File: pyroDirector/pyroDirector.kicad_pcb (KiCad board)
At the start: 2 copper layers, 100 x 100 mm, 92 parts, among them J1 AudioJack3.5mm, J10 PWR_CONN, J11 CALIB_MODULE, J12 DISP_I2C, J13 Conn_01x03_Male, J14 SJ1-2503A, J15 Conn_01x03_Male, J16 SJ1-2503A, J17 Conn_01x03_Male, J18 SJ1-2503A, J19 LED_ext, J2 Header_A1-A15, J20 Screw_Terminal_01x02, J21 LED_ext, J22 Screw_Terminal_01x02, J23 LED_ext, J24 Screw_Terminal_01x02, J3 Header_D14-19, J4 Header_D48-53, J5 V_Batt, J6 Header_ISP, J7 PWR_SWITCH, J8 Batt, J9 Conn_01x07_Male, K1 PR12-5V-360-1C, K2 PR12-5V-360-1C, K3 PR12-5V-360-1C, Q1 MMBT2222A 1P, Q10 MMBT2222A 1P, Q11 IRLB8721PbF, Q12 MMBT2222A 1P, Q13 IRLB8721PbF, Q2 MMBT2222A 1P, Q3 MMBT2222A 1P, Q4 MMBT2222A 1P, Q5 MMBT2222A 1P, Q6 MMBT2222A 1P, Q7 MMBT2222A 1P, Q8 MMBT2222A 1P, Q9 IRLB8721PbF, SW1 SW_SPDT, U1 MEGA_PRO_ATMEGA2560

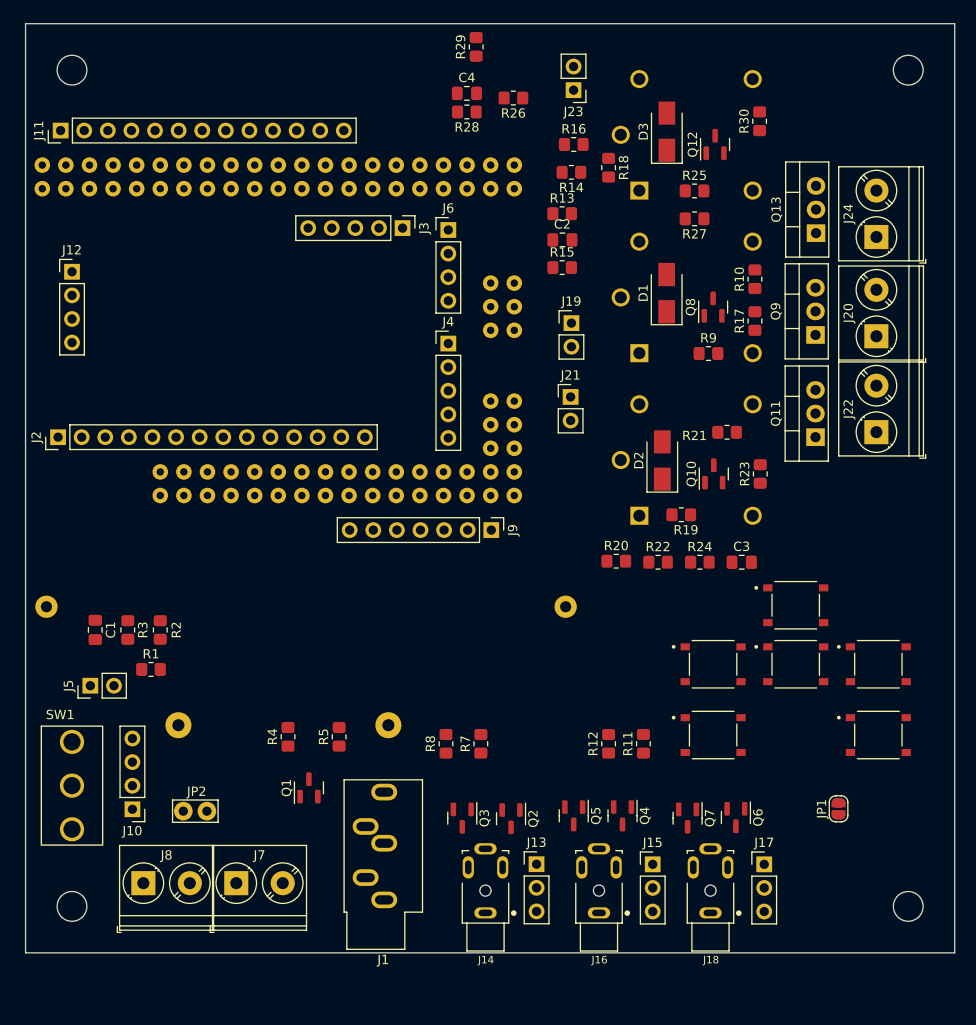
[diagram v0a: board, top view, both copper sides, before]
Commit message: placement improvements, added missing header -->should we use handsolder pads?
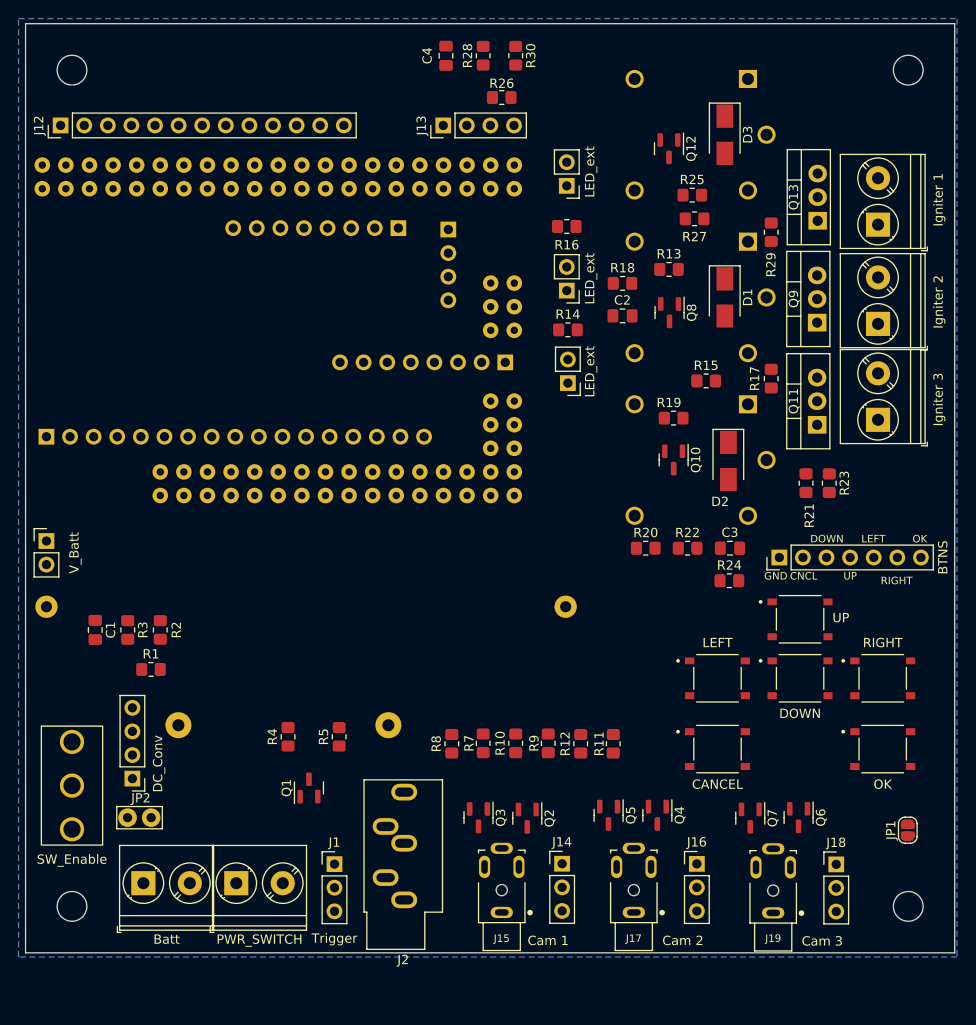
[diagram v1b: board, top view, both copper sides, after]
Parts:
- added J1: Conn_01x03_Male, Connector_PinHeader_2.54mm:PinHeader_1x03_P2.54mm_Vertical, F.Cu at (130.0, 133.0)
- J10: renamed from J9; value Conn_01x07_Male -> BTNS
- J11: renamed from J10; value PWR_CONN -> DC_Conv
- J3: renamed from J2; footprint Connector_PinHeader_2.54mm:PinHeader_1x14_P2.54mm_Vertical -> Connector_PinHeader_2.54mm:PinHeader_1x17_P2.54mm_Vertical; moved to B.Cu
- J4: renamed from J3; footprint Connector_PinHeader_2.54mm:PinHeader_1x05_P2.54mm_Vertical -> Connector_PinHeader_2.54mm:PinHeader_1x08_P2.54mm_Vertical; moved to B.Cu
- J5: renamed from J4; footprint Connector_PinHeader_2.54mm:PinHeader_1x05_P2.54mm_Vertical -> Connector_PinHeader_2.54mm:PinHeader_1x08_P2.54mm_Vertical; moved to B.Cu
- J7: renamed from J6; moved to B.Cu
- JP2: value Jumper_2_Bridged -> Arduino_PWR
- SW1: value SW_SPDT -> SW_Enable
- moved R10 56.2 mm to (149.5, 120.0)
- moved R9 45.4 mm to (153.0, 120.0), turned to -90 degrees
- moved J13 42.9 mm to (141.7, 53.5), turned to 90 degrees
- moved R29 37.5 mm to (177.0, 65.0), turned to -90 degrees
- moved J10 31.1 mm to (177.9, 100.0), turned to 90 degrees
- moved R30 27.2 mm to (149.5, 46.0), turned to -90 degrees
- moved R15 19.7 mm to (170.0, 81.0)
- moved R14 17.0 mm to (155.1, 75.5), turned to 0 degrees
- moved J6 16.3 mm to (99.0, 98.2), turned to 0 degrees
- moved K3 15.7 mm to (176.5, 54.5), turned to 180 degrees
- moved K1 15.7 mm to (176.5, 72.0), turned to 180 degrees
- moved K2 15.7 mm to (176.5, 89.5), turned to 180 degrees
- moved R13 13.0 mm to (166.0, 69.0)
- moved R18 12.5 mm to (161.0, 70.5), turned to 0 degrees
- moved R19 10.4 mm to (166.5, 85.0), turned to 0 degrees
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- renumbered J11 to J12, J12 to J13, J13 to J14, J14 to J15, J15 to J16, J16 to J17, J17 to J18, J18 to J19, J1 to J2, J19 to J20, J20 to J21, J21 to J22, J22 to J23, J23 to J24, J24 to J25, J5 to J6, J7 to J8, J8 to J9, K2 to K1, K3 to K2, K1 to K3
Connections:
- J20 pad 2: Net-(J19-Pad2) -> Net-(J20-Pad2)
- J21 pad 1: Net-(J20-Pad1) -> Net-(J20-Pad2)
- J21 pad 2: Net-(J19-Pad2) -> Net-(J21-Pad2)
- J22 pad 2: Net-(J21-Pad2) -> Net-(J22-Pad2)
- J23 pad 1: Net-(J22-Pad1) -> Net-(J22-Pad2)
- J23 pad 2: Net-(J21-Pad2) -> Net-(J23-Pad2)
- J24 pad 2: Net-(J23-Pad2) -> Net-(J24-Pad2)
- J25 pad 1: Net-(J24-Pad1) -> Net-(J24-Pad2)
- J25 pad 2: Net-(J23-Pad2) -> Net-(J25-Pad2)
- JP2 pad 1: /VO+ -> +5V
- K1 pad COM: Net-(J20-Pad1) -> Net-(J21-Pad2)
- K1 pad NC: Net-(J19-Pad2) -> Net-(J20-Pad2)
- K2 pad COM: Net-(J22-Pad1) -> Net-(J23-Pad2)
- K2 pad NC: Net-(J21-Pad2) -> Net-(J22-Pad2)
- K3 pad COM: Net-(J24-Pad1) -> Net-(J25-Pad2)
- K3 pad NC: Net-(J23-Pad2) -> Net-(J24-Pad2)
- Q11 pad 2: Net-(J21-Pad2) -> Net-(J22-Pad2)
- Q13 pad 2: Net-(J23-Pad2) -> Net-(J24-Pad2)
- Q9 pad 2: Net-(J19-Pad2) -> Net-(J20-Pad2)
- R14 pad 1: Net-(J19-Pad2) -> Net-(J20-Pad2)
- R20 pad 1: Net-(J21-Pad2) -> Net-(J22-Pad2)
- R26 pad 1: Net-(J23-Pad2) -> Net-(J24-Pad2)
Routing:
- added copper zone on In1.Cu, net +5V
- added copper zone on In2.Cu, net 12V_LTD
- added copper zone on B.Cu, net GND
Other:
- copper layers 2 -> 4
- board text added: "CNCL"
- board text added: "Cam 1"
- board text added: "Cam 2"
- board text added: "Cam 3"
- board text added: "GND"
- board text added: "Trigger"
- board text removed: "Cam_1"
- board text removed: "Cam_2"
- board text removed: "Cam_3"

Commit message: placement & 3-D models complete
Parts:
- removed J5: Header_D48-53, Connector_PinHeader_2.54mm:PinHeader_1x08_P2.54mm_Vertical
- F1, J3, J7, R6: moved to F.Cu
- J11: moved to B.Cu
- J4: value Header_D14-19 -> Header_D14-19_D49_51_53; footprint Connector_PinHeader_2.54mm:PinHeader_1x08_P2.54mm_Vertical -> Connector_PinHeader_2.54mm:PinHeader_1x11_P2.54mm_Vertical; moved to F.Cu
- JP2: footprint TestPoint:TestPoint_Bridge_Pitch2.54mm_Drill1.0mm -> Connector_PinHeader_2.54mm:PinHeader_1x02_P2.54mm_Vertical
- moved R24 25.3 mm to (152.5, 87.0), turned to -90 degrees
- moved R22 22.6 mm to (152.5, 82.5), turned to 90 degrees
- moved C3 20.5 mm to (156.0, 87.0), turned to -90 degrees
- moved R20 18.1 mm to (156.0, 82.5), turned to -90 degrees
- moved R1 17.9 mm to (100.5, 97.0)
- moved C1 17.1 mm to (99.0, 91.5)
- moved R2 17.1 mm to (106.0, 91.5)
- moved R3 17.1 mm to (102.5, 91.5)
- moved JP2 16.1 mm to (105.8, 112.5), turned to -90 degrees
- moved JP1 15.9 mm to (177.0, 123.4), turned to -90 degrees
- moved Q5 11.3 mm to (158.0, 139.0), turned to 0 degrees
- moved Q7 11.0 mm to (174.5, 139.0), turned to 0 degrees
- moved J6 10.3 mm to (99.5, 108.5), turned to 180 degrees
- moved Q4 9.20 mm to (158.0, 134.0), turned to 0 degrees
- moved R5 8.53 mm to (139.0, 120.0)
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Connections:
- J4 pad 2: /D19 -> /D53
- J4 pad 3: /D18 -> /D51
- J4 pad 4: /D17 -> /D49
- J4 pad 5: /D16 -> /D19
- J4 pad 6: /D15 -> /D18
- J4 pad 7: /D14 -> /D17
- J4 pad 8: GND -> /D16
- JP2 pad 1: +5V -> /VO+
- U1 pad D26: /FIRE_1 -> unconnected-(U1-PadD26)
- U1 pad D28: /PRIME_2 -> unconnected-(U1-PadD28)
- U1 pad D30: /SENSE_2 -> unconnected-(U1-PadD30)
- U1 pad D32: /BTN_OK -> /TRIGGER_LED
- U1 pad D33: /BTN_UP -> /TRIGGER
- U1 pad D34: /BTN_DOWN -> /PRE_CAM_0
- U1 pad D35: /BTN_RIGHT -> /SHUTTER_CAM_0
- U1 pad D36: /BTN_LEFT -> /PRE_CAM_1
- U1 pad D37: /BTN_CNCL -> /SHUTTER_CAM_1
- U1 pad D38: /TRIGGER_LED -> /PRE_CAM_2
- U1 pad D39: /TRIGGER -> /SHUTTER_CAM_2
- U1 pad D40: unconnected-(U1-PadD40) -> /BTN_OK
- U1 pad D41: unconnected-(U1-PadD41) -> /BTN_UP
- U1 pad D42: /PRE_CAM_0 -> /BTN_DOWN
- U1 pad D43: /SHUTTER_CAM_0 -> /BTN_RIGHT
- U1 pad D44: /PRE_CAM_1 -> /BTN_LEFT
- U1 pad D45: /SHUTTER_CAM_1 -> /BTN_CNCL
- U1 pad D46: /PRE_CAM_2 -> unconnected-(U1-PadD46)
- U1 pad D47: /SHUTTER_CAM_2 -> unconnected-(U1-PadD47)
- U1 pad D48: /D48 -> /SENSE_2
- U1 pad D50: /D50 -> /PRIME_2
- U1 pad D52: /D52 -> /FIRE_1
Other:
- board text added: "EN"
- board text added: "Vin+"
- board text added: "Vo+"

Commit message: layout in progress
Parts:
- H1, H2, H3, H4: footprint MountingHole:MountingHole_3.2mm_M3 -> MountingHole:MountingHole_3.2mm_M3_Pad_Via
- moved R16 14.0 mm to (154.2, 75.0)
- moved R19 9.55 mm to (166.5, 90.5), turned to 90 degrees
- moved Q1 9.28 mm to (139.2, 125.5)
- moved R4 9.28 mm to (134.7, 125.5)
- moved J13 9.17 mm to (136.5, 46.0), turned to 0 degrees
- moved R25 8.05 mm to (162.2, 52.8), turned to 90 degrees
- moved J22 7.93 mm to (154.0, 86.0)
- moved C3 6.01 mm to (161.8, 88.8)
- moved R20 6.01 mm to (161.8, 84.2)
- moved R22 6.01 mm to (158.2, 84.2)
- moved R24 6.01 mm to (158.2, 88.8)
- moved R9 3.62 mm to (149.4, 120.0)
- moved R12 3.50 mm to (160.0, 120.0)
- moved J3 3.50 mm to (100.2, 81.0)
- moved R10 3.50 mm to (153.0, 120.0)
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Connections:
- U1 pad D22: /PRIME_0 -> unconnected-(U1-PadD22)
- U1 pad D23: /FIRE_0 -> /SENSE_0
- U1 pad D24: /SENSE_0 -> unconnected-(U1-PadD24)
- U1 pad D25: /PRIME_1 -> unconnected-(U1-PadD25)
- U1 pad D26: unconnected-(U1-PadD26) -> /SENSE_1
- U1 pad D27: /SENSE_1 -> unconnected-(U1-PadD27)
- U1 pad D28: unconnected-(U1-PadD28) -> /PRIME_1
- U1 pad D29: /FIRE_2 -> unconnected-(U1-PadD29)
- U1 pad D30: unconnected-(U1-PadD30) -> /FIRE_0
- U1 pad D31: unconnected-(U1-PadD31) -> /PRIME_0
- U1 pad D43: /BTN_RIGHT -> unconnected-(U1-PadD43)
- U1 pad D46: unconnected-(U1-PadD46) -> /BTN_RIGHT
- U1 pad D47: unconnected-(U1-PadD47) -> /FIRE_2
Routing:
- net /BTN_OK: track 0.00 -> 89.3 mm, vias 0 -> 2
- net Net-(JP1-Pad1): track 0.00 -> 74.2 mm
- net /BTN_DOWN: track 0.00 -> 72.2 mm, vias 0 -> 2
- net /BTN_CNCL: track 0.00 -> 68.4 mm
- net /BTN_RIGHT: track 0.00 -> 62.8 mm, vias 0 -> 4
- net GND: track 0.00 -> 62.6 mm, vias 0 -> 12
- net /BTN_LEFT: track 0.00 -> 60.9 mm, vias 0 -> 6
- net /BTN_UP: track 0.00 -> 55.3 mm, vias 0 -> 4
- net Net-(J24-Pad2): track 0.00 -> 50.8 mm
- net Net-(J20-Pad2): track 0.00 -> 47.6 mm, vias 0 -> 2
- net +12V: track 0.00 -> 42.1 mm
- net Net-(J22-Pad2): track 0.00 -> 41.0 mm
- net /SHUTTER_CAM_2: track 0.00 -> 37.1 mm
- net /TRIGGER_LED: track 0.00 -> 35.5 mm
- net /SHUTTER_CAM_1: track 0.00 -> 35.0 mm
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- added copper zone on In2.Cu, net +12V
- added copper zone on In2.Cu, net Net-(F1-Pad1)
- added copper zone on In2.Cu, net Net-(J24-Pad2)
- added copper zone on In2.Cu, net Net-(J25-Pad2)
- added copper zone on In2.Cu, net Net-(J8-Pad1)
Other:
- outline, holes or cut-outs redrawn

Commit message: final design
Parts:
- moved R17 1.06 mm to (177.5, 76.0)
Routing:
- net /BTN_DOWN: track 72.2 -> 78.2 mm
- net /LED_1: track 20.6 -> 20.1 mm
- added copper zone on In1.Cu, net Net-(J20-Pad2)
- added copper zone on In1.Cu, net Net-(J21-Pad2)
- added copper zone on In2.Cu, net Net-(J21-Pad2)
- added copper zone on In1.Cu, net Net-(J23-Pad2)
- added copper zone on In2.Cu, net Net-(J23-Pad2)
- added copper zone on In1.Cu, net Net-(J24-Pad2)
- added copper zone on In1.Cu, net Net-(J25-Pad2)
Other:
- board text added: "MISO"
- board text added: "MOSI"
- board text added: "RST"
- board text added: "SCK"

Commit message: Manufactured 2021-02-25
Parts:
- D1, D2, D3: value SM4007 -> M7
- S4: value PCB_Btn_OK -> PCB_Btn_LEFT
- S5: value PCB_Btn_OK -> PCB_Btn_RIGHT
